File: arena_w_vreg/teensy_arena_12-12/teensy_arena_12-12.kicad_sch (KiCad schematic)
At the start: 9 parts, among them J2 Conn_01x04_Pin, J3 Conn_01x04_Pin, Q2 MOSFET_NCHAN

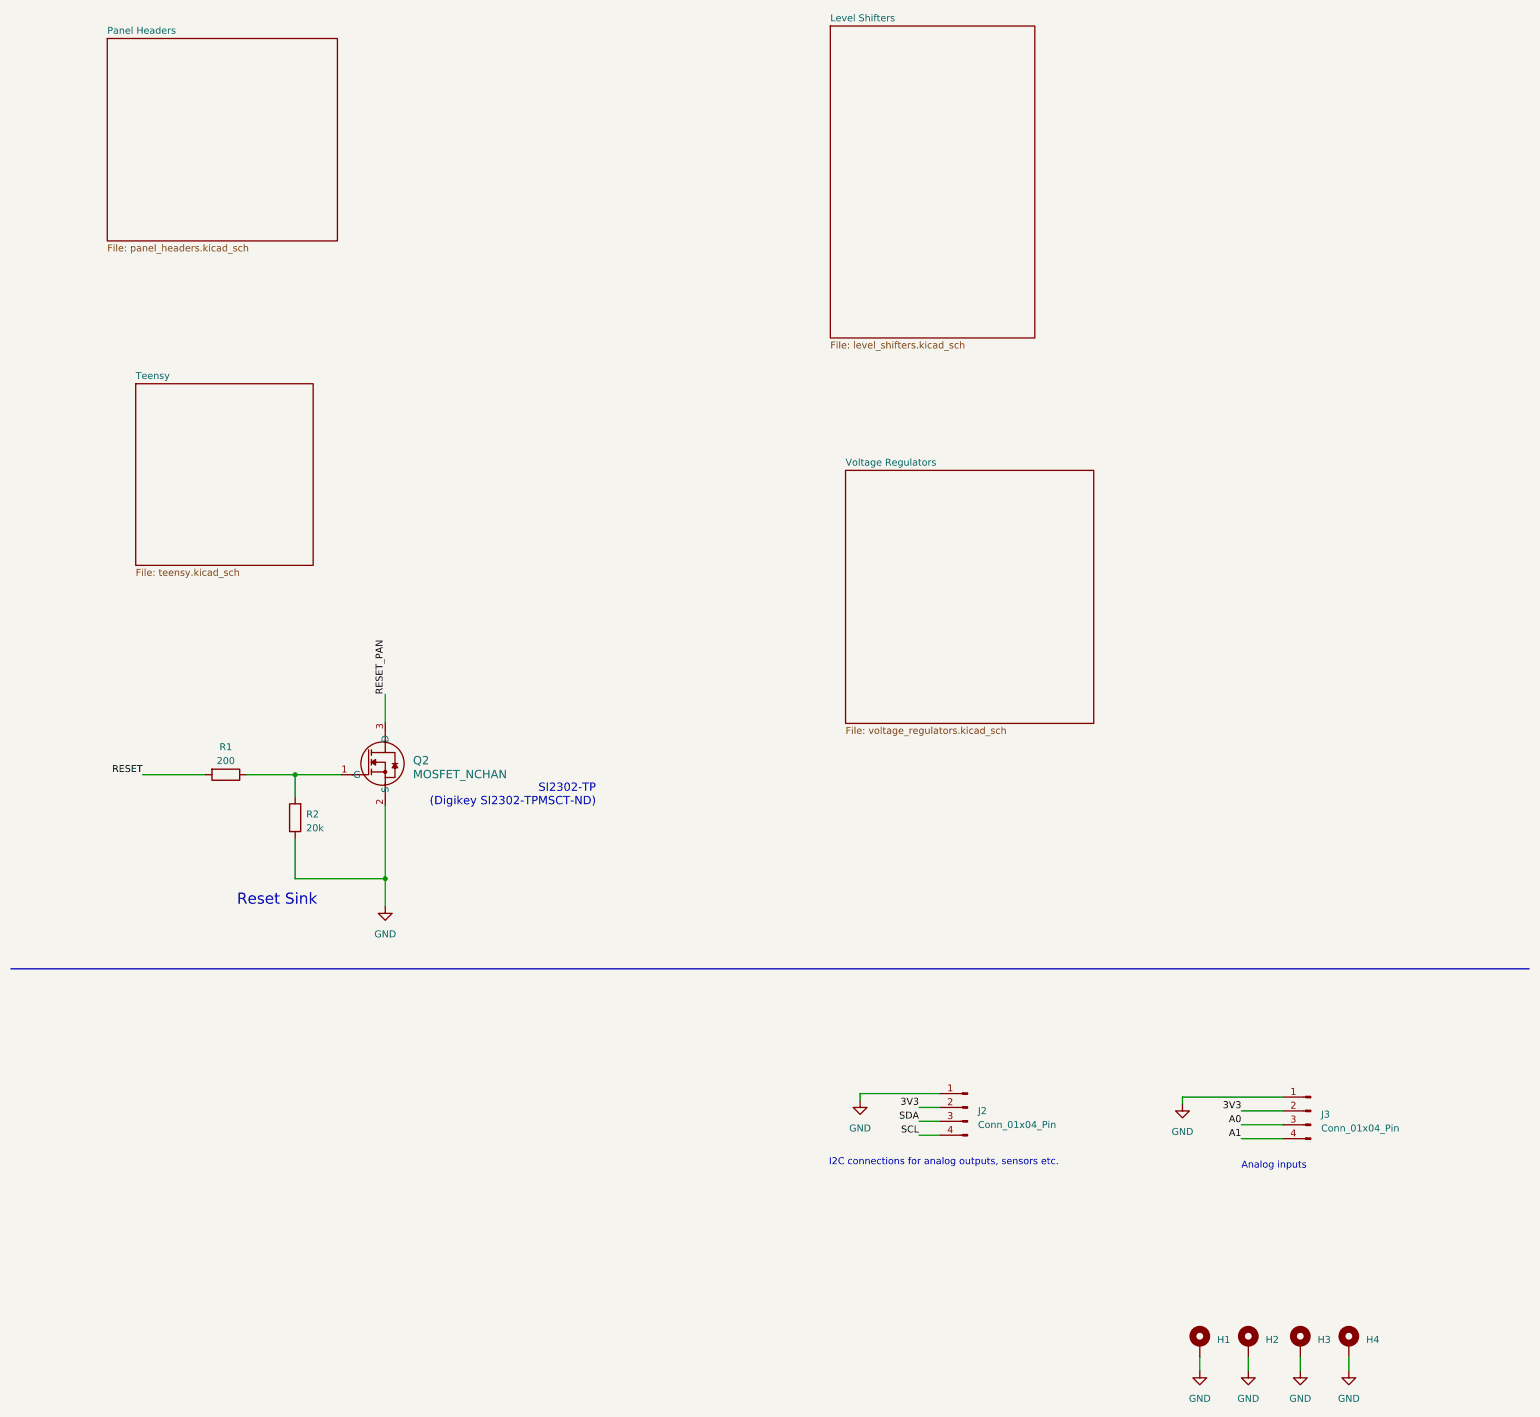
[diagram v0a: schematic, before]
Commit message: Worked on 12-12 teensy arena with voltage regulator.
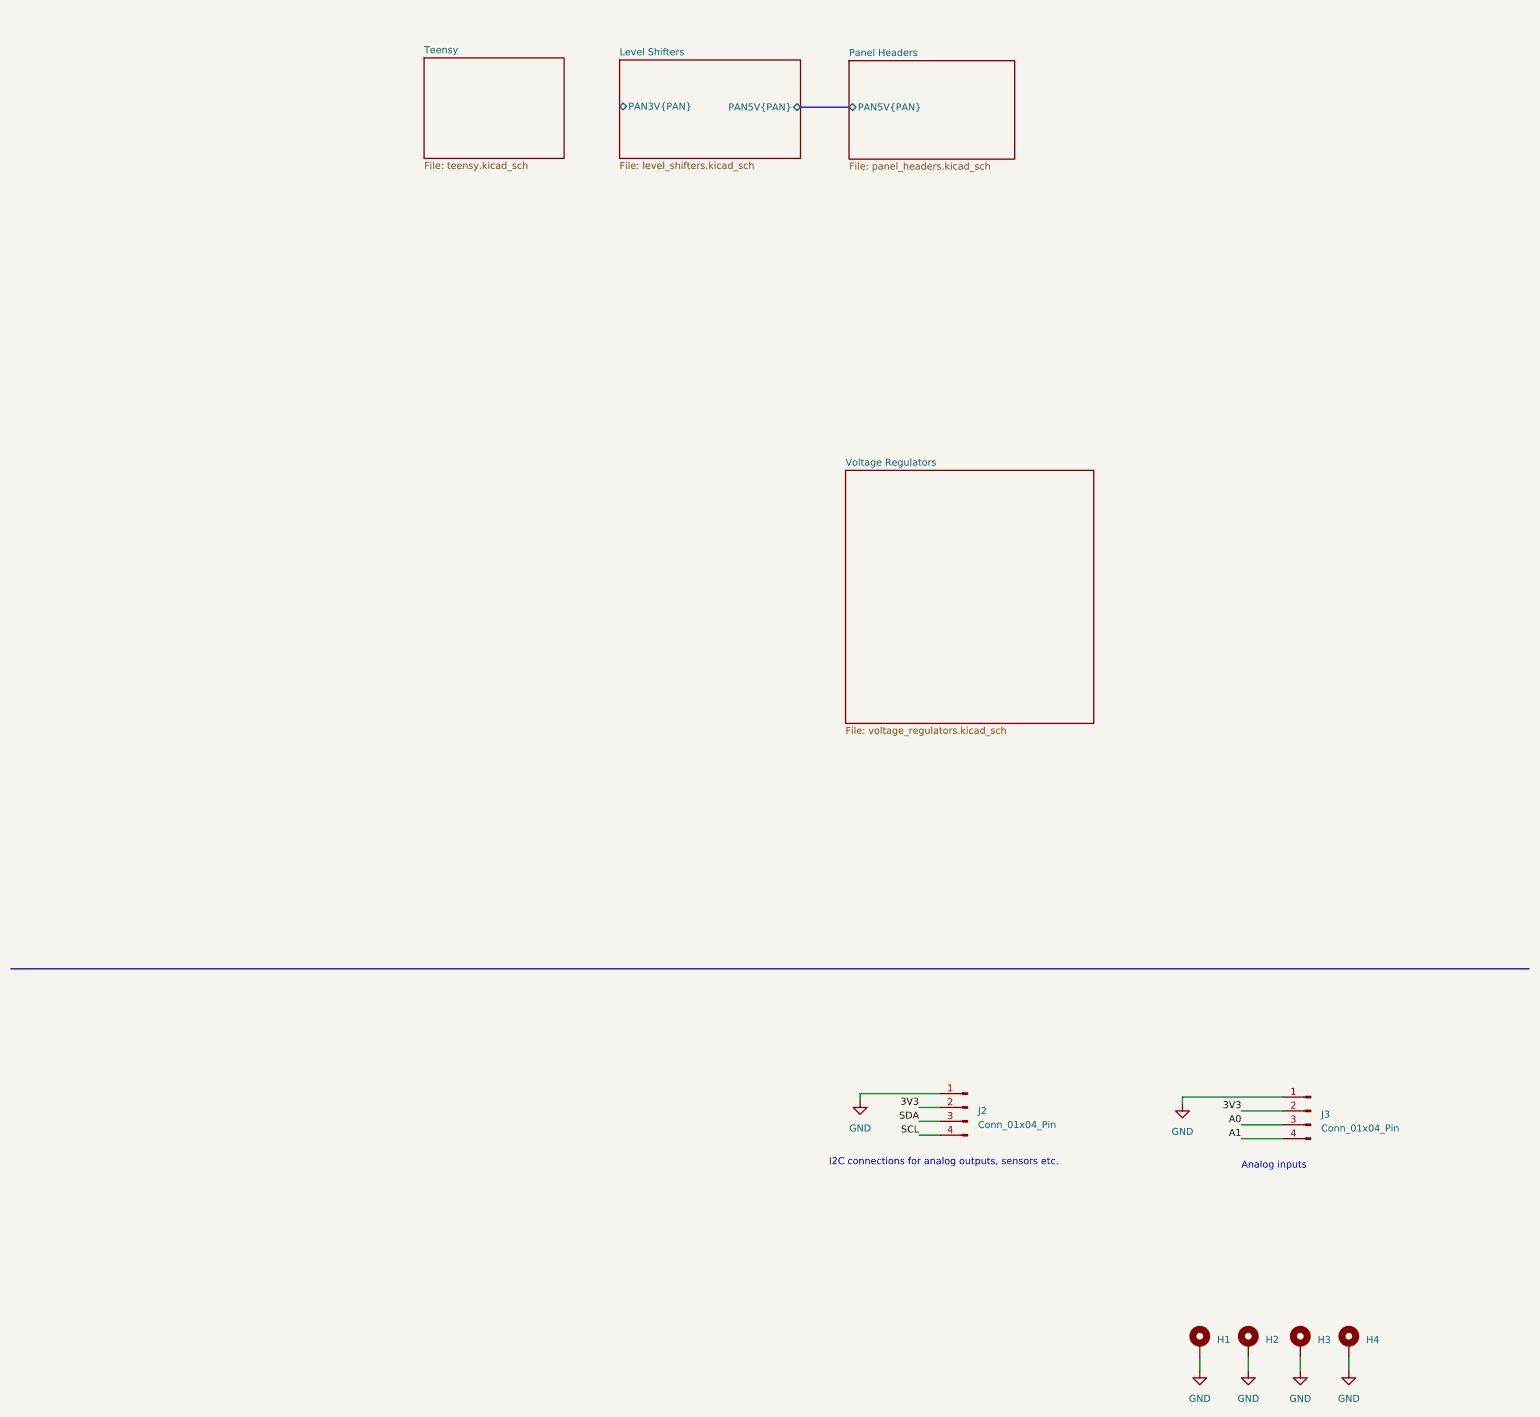
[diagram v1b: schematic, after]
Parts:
- removed Q2: MOSFET_NCHAN, Package_TO_SOT_SMD:SOT-23-3, symbol arena_custom:MOSFET_NCHAN
- removed R1: 200, Resistor_SMD:R_0805_2012Metric, symbol Device:R
- removed R2: 20k, Resistor_SMD:R_0805_2012Metric, symbol Device:R
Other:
- sheet Level Shifters ports: added PAN3V{PAN}, PAN5V{PAN}; removed none
- sheet Panel Headers ports: added PAN5V{PAN}; removed none
- note removed: "Reset Sink"
- note removed: "SI2302-TP (Digikey SI2302-TPMSCT-ND)"
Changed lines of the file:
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@@
     (date "11 jun 2015")
   )
-  (junction (at 64.77 163.83) (diameter 0) (color 0 0 0 0)
-  )
-  (junction (at 81.28 182.88) (diameter 0) (color 0 0 0 0)
-  )
   (wire (pts (xy 179.07 224.79) (xy 182.88 224.79))
     (stroke (width 0) (type default))
@@
     (stroke (width 0) (type default))
   )
+  (bus (pts (xy 157.353 41.529) (xy 166.243 41.529))
+    (stroke (width 0) (type default))
+  )
   (wire (pts (xy 168.275 222.25) (xy 168.275 223.52))
     (stroke (width 0) (type default))
@@
     (stroke (width 0) (type default))
   )
-  (wire (pts (xy 64.77 182.88) (xy 81.28 182.88))
-    (stroke (width 0) (type default))
-  )
   (wire (pts (xy 230.505 270.51) (xy 230.505 273.05))
     (stroke (width 0) (type default))
@@
     (stroke (width 0) (type default))
   )
-  (wire (pts (xy 36.83 163.83) (xy 48.26 163.83))
-    (stroke (width 0) (type default))
-  )
-  (wire (pts (xy 55.88 163.83) (xy 64.77 163.83))
-    (stroke (width 0) (type default))
-  )
   (wire (pts (xy 248.92 270.51) (xy 248.92 273.05))
     (stroke (width 0) (type default))
   )
-  (wire (pts (xy 81.28 182.88) (xy 81.28 187.96))
-    (stroke (width 0) (type default))
-  )
   (wire (pts (xy 238.125 227.965) (xy 245.745 227.965))
     (stroke (width 0) (type default))
   )
-  (wire (pts (xy 64.77 163.83) (xy 64.77 167.894))
-    (stroke (width 0) (type default))
-  )
   (wire (pts (xy 238.125 230.505) (xy 245.745 230.505))
     (stroke (width 0) (type default))
@@
     (stroke (width 0) (type default))
   )
-  (wire (pts (xy 64.77 175.514) (xy 64.77 182.88))
-    (stroke (width 0) (type default))
-  )
-  (wire (pts (xy 64.77 163.83) (xy 73.152 163.83))
-    (stroke (width 0) (type default))
-  )
-  (wire (pts (xy 81.28 169.418) (xy 81.28 182.88))
-    (stroke (width 0) (type default))
-  )
-  (wire (pts (xy 81.28 154.305) (xy 81.28 149.098))
-    (stroke (width 0) (type default))
-  )
   (wire (pts (xy 238.125 225.425) (xy 245.745 225.425))
     (stroke (width 0) (type default))
-  )
-  (text "SI2302-TP \n(Digikey SI2302-TPMSCT-ND)" (at 119.888 169.672 0)
-    (effects (font (size 1.524 1.524)) (justify right bottom))
   )
   (text "Analog inputs" (at 238.125 236.22 0)
@@
   )
   (text "I2C connections for analog outputs, sensors etc. " (at 162.56 235.585 0)
-    (effects (font (size 1.27 1.27)) (justify left bottom))
-  )
-  (text "Reset Sink" (at 54.102 187.96 0)
-    (effects (font (size 2.032 2.032)) (justify left bottom))
-  )
-  (label "RESET" (at 36.83 163.83 180) (fields_autoplaced)
-    (effects (font (size 1.27 1.27)) (justify right bottom))
-  )
-  (label "RESET_PAN" (at 81.28 149.098 90) (fields_autoplaced)
     (effects (font (size 1.27 1.27)) (justify left bottom))
   )
@@
     )
   )
-  (symbol (lib_id "arena_custom:MOSFET_NCHAN") (at 81.28 163.83 0) (unit 1)
-    (in_bom yes) (on_board yes) (dnp no) (fields_autoplaced)
-    (property "Reference" "Q2" (at 86.36 161.2265 0)
-      (effects (font (size 1.524 1.524)) (justify left))
-    )
-    (property "Value" "MOSFET_NCHAN" (at 86.36 163.7665 0)
-      (effects (font (size 1.524 1.524)) (justify left))
-    )
-    (property "Footprint" "Package_TO_SOT_SMD:SOT-23-3" (at 81.28 161.544 0)
-      (effects (font (size 1.524 1.524)) hide)
-    )
-    (property "Datasheet" "" (at 81.28 161.544 0)
-      (effects (font (size 1.524 1.524)))
-    )
-    (pin "1")
-    (pin "2")
-    (pin "3")
-    (instances
-      (project "teensy_arena_12-12"
-        (path "/a2511654-3a17-43f1-8b9e-c45e375533dc"
-          (reference "Q2") (unit 1)
-        )
-      )
-    )
-  )
-  (symbol (lib_id "Device:R") (at 64.77 171.704 180) (unit 1)
-    (in_bom yes) (on_board yes) (dnp no) (fields_autoplaced)
-    (property "Reference" "R2" (at 66.802 171.069 0)
-      (effects (font (size 1.27 1.27)) (justify right))
-    )
-    (property "Value" "20k" (at 66.802 173.609 0)
-      (effects (font (size 1.27 1.27)) (justify right))
-    )
-    (property "Footprint" "Resistor_SMD:R_0805_2012Metric" (at 66.548 171.704 90)
-      (effects (font (size 1.27 1.27)) hide)
-    )
-    (property "Datasheet" "~" (at 64.77 171.704 0)
-      (effects (font (size 1.27 1.27)) hide)
-    )
-    (pin "1")
-    (pin "2")
-    (instances
-      (project "teensy_arena_12-12"
-        (path "/a2511654-3a17-43f1-8b9e-c45e375533dc"
-          (reference "R2") (unit 1)
-        )
-      )
-    )
-  )
   (symbol (lib_id "power:GND") (at 248.92 273.05 0) (mirror y) (unit 1)
     (in_bom yes) (on_board yes) (dnp no) (fields_autoplaced)
@@
     )
   )
-  (symbol (lib_id "Device:R") (at 52.07 163.83 270) (unit 1)
-    (in_bom yes) (on_board yes) (dnp no) (fields_autoplaced)
-    (property "Reference" "R1" (at 52.07 158.75 90)
-      (effects (font (size 1.27 1.27)))
-    )
-    (property "Value" "200" (at 52.07 161.29 90)
-      (effects (font (size 1.27 1.27)))
-    )
-    (property "Footprint" "Resistor_SMD:R_0805_2012Metric" (at 52.07 162.052 90)
-      (effects (font (size 1.27 1.27)) hide)
-    )
-    (property "Datasheet" "~" (at 52.07 163.83 0)
-      (effects (font (size 1.27 1.27)) hide)
-    )
-    (pin "1")
-    (pin "2")
-    (instances
-      (project "teensy_arena_12-12"
-        (path "/a2511654-3a17-43f1-8b9e-c45e375533dc"
-          (reference "R1") (unit 1)
-        )
-      )
-    )
-  )
   (symbol (lib_id "power:GND") (at 227.33 224.155 0) (mirror y) (unit 1)
     (in_bom yes) (on_board yes) (dnp no) (fields_autoplaced)
@@
         (path "/a2511654-3a17-43f1-8b9e-c45e375533dc"
           (reference "#PWR07") (unit 1)
-        )
-      )
-    )
-  )
-  (symbol (lib_id "power:GND") (at 81.28 187.96 0) (unit 1)
-    (in_bom yes) (on_board yes) (dnp no) (fields_autoplaced)
-    (property "Reference" "#PWR035" (at 81.28 194.31 0)
-      (effects (font (size 1.27 1.27)) hide)
-    )
-    (property "Value" "GND" (at 81.28 193.04 0)
-      (effects (font (size 1.27 1.27)))
-    )
-    (property "Footprint" "" (at 81.28 187.96 0)
-      (effects (font (size 1.27 1.27)) hide)
-    )
-    (property "Datasheet" "" (at 81.28 187.96 0)
-      (effects (font (size 1.27 1.27)) hide)
-    )
-    (pin "1")
-    (instances
-      (project "teensy_arena_12-12"
-        (path "/a2511654-3a17-43f1-8b9e-c45e375533dc"
-          (reference "#PWR035") (unit 1)
         )
       )
@@
     )
   )
-  (sheet (at 162.814 26.67) (size 37.465 57.15) (fields_autoplaced)
+  (sheet (at 124.206 32.893) (size 33.147 18.034) (fields_autoplaced)
     (stroke (width 0.1524) (type solid))
     (fill (color 0 0 0 0.0000))
-    (property "Sheetname" "Level Shifters" (at 162.814 25.9584 0)
+    (property "Sheetname" "Level Shifters" (at 124.206 32.1814 0)
       (effects (font (size 1.27 1.27)) (justify left bottom))
     )
-    (property "Sheetfile" "level_shifters.kicad_sch" (at 162.814 84.4046 0)
+    (property "Sheetfile" "level_shifters.kicad_sch" (at 124.206 51.5116 0)
       (effects (font (size 1.27 1.27)) (justify left top))
     )
+    (pin "PAN5V{PAN}" bidirectional (at 157.353 41.529 0)
+      (effects (font (size 1.27 1.27)) (justify right))
+    )
+    (pin "PAN3V{PAN}" bidirectional (at 124.206 41.402 180)
+      (effects (font (size 1.27 1.27)) (justify left))
+    )
     (instances
       (project "teensy_arena_12-12"
@@
     )
   )
-  (sheet (at 35.56 92.202) (size 32.512 33.274) (fields_autoplaced)
+  (sheet (at 88.392 32.512) (size 25.654 18.415) (fields_autoplaced)
     (stroke (width 0.1524) (type solid))
     (fill (color 0 0 0 0.0000))
-    (property "Sheetname" "Teensy" (at 35.56 91.4904 0)
+    (property "Sheetname" "Teensy" (at 88.392 31.8004 0)
       (effects (font (size 1.27 1.27)) (justify left bottom))
     )
-    (property "Sheetfile" "teensy.kicad_sch" (at 35.56 126.0606 0)
+    (property "Sheetfile" "teensy.kicad_sch" (at 88.392 51.5116 0)
       (effects (font (size 1.27 1.27)) (justify left top))
     )
@@
     )
   )
-  (sheet (at 30.353 28.956) (size 42.164 37.084) (fields_autoplaced)
+  (sheet (at 166.243 33.02) (size 30.353 18.034) (fields_autoplaced)
     (stroke (width 0.1524) (type solid))
     (fill (color 0 0 0 0.0000))
-    (property "Sheetname" "Panel Headers" (at 30.353 28.2444 0)
+    (property "Sheetname" "Panel Headers" (at 166.243 32.3084 0)
       (effects (font (size 1.27 1.27)) (justify left bottom))
     )
-    (property "Sheetfile" "panel_headers.kicad_sch" (at 30.353 66.6246 0)
+    (property "Sheetfile" "panel_headers.kicad_sch" (at 166.243 51.6386 0)
       (effects (font (size 1.27 1.27)) (justify left top))
     )
-    (instances
+    (pin "PAN5V{PAN}" bidirectional (at 166.243 41.529 180)
+      (effects (font (size 1.27 1.27)) (justify left))
+    )
+    (instances
